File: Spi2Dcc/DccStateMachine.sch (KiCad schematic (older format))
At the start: 9 parts, among them U302 74HC32, U401 74HC163, U402 74HC04, U403 74HC163, U404 74HC193

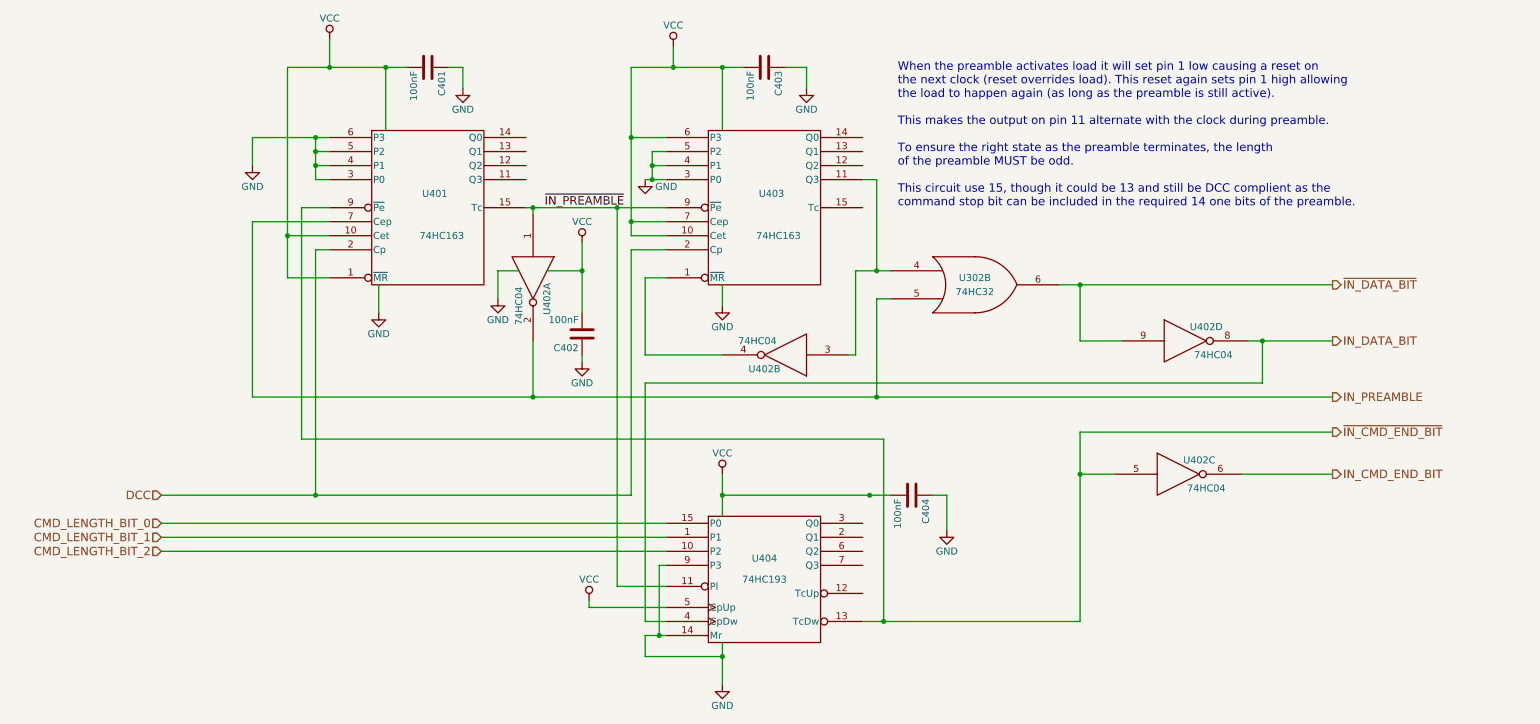
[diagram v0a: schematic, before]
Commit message: Fixed missing connection from U404 to VCC in DccStateMachine schematic. Schematic revision updated to 1.4, pcb not yet.
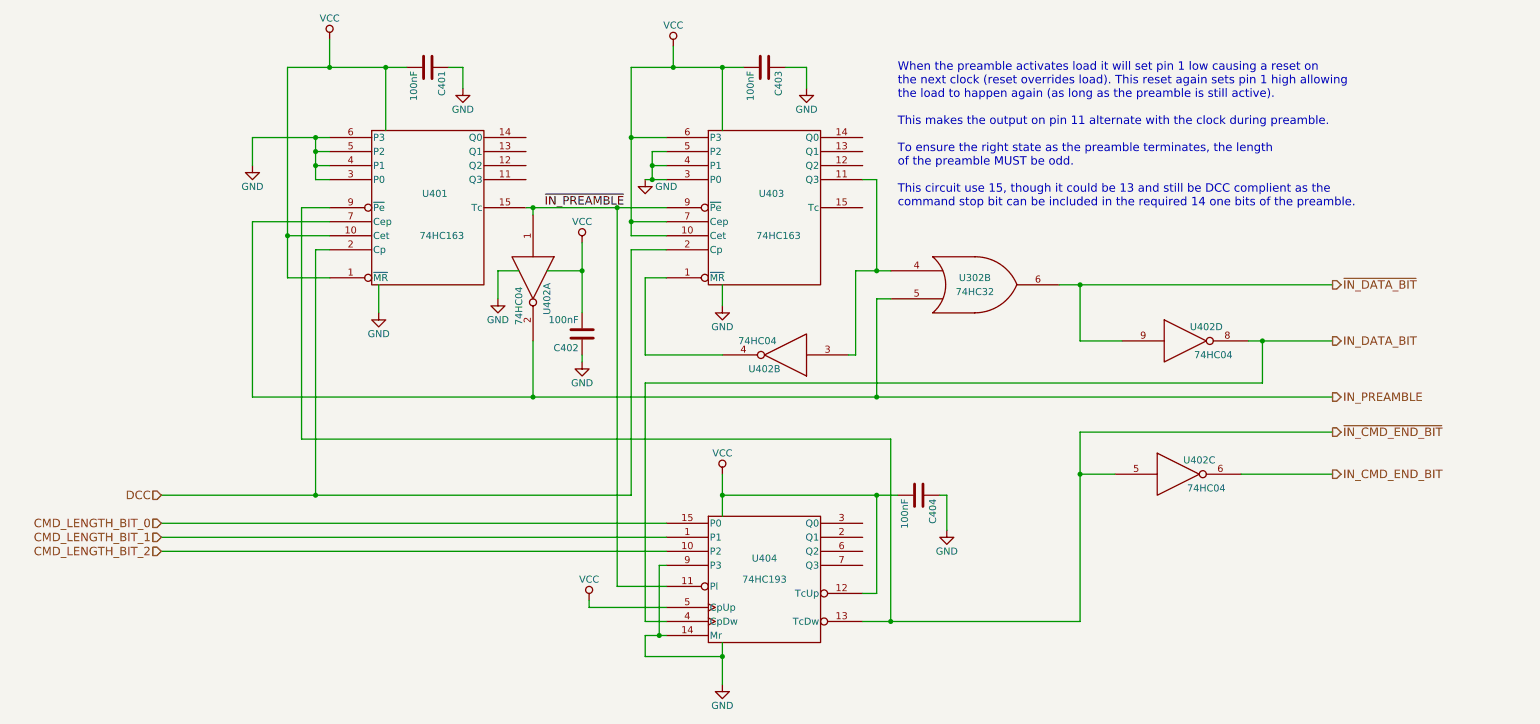
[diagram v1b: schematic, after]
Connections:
- net VCC: now also U404.12 (TcUp)
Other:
- moved on the sheet: C404
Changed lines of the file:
@@
 Sheet 4 9
 Title "Trainiot SPI DCC"
-Date "2017-03-27"
-Rev "1.3"
+Date "2017-04-26"
+Rev "1.4"
 Comp "Lars Møllebjerg"
 Comment1 "The CMD_LENGTH_BITs are used to determine when to generate the command end bit."
@@
 L C C404
 U 1 1 58B3E4A2
-P 7100 4600
-F 0 "C404" H 7125 4700 50  0000 L CNN
-F 1 "100nF" H 7125 4500 50  0000 L CNN
-F 2 "Capacitors_SMD:C_0603" H 7138 4450 50  0001 C CNN
-F 3 "" H 7100 4600 50  0000 C CNN
-	1    7100 4600
+P 7150 4600
+F 0 "C404" H 7175 4700 50  0000 L CNN
+F 1 "100nF" H 7175 4500 50  0000 L CNN
+F 2 "Capacitors_SMD:C_0603" H 7188 4450 50  0001 C CNN
+F 3 "" H 7150 4600 50  0000 C CNN
+	1    7150 4600
 	0    1    1    0
 $EndComp
@@
 	2950 1350 2950 1550
 Wire Wire Line
-	2650 1550 3500 1550
+	2650 1550 2950 1550
+Wire Wire Line
+	2950 1550 3350 1550
+Wire Wire Line
+	3350 1550 3500 1550
 Wire Wire Line
 	3350 1550 3350 2000
 Wire Wire Line
-	2650 1550 2650 3050
+	2650 1550 2650 2750
+Wire Wire Line
+	2650 2750 2650 3050
 Connection ~ 2950 1550
 Wire Wire Line
@@
 	3300 3100 3300 3300
 Wire Wire Line
-	2400 2050 2950 2050
+	2400 2050 2850 2050
+Wire Wire Line
+	2850 2050 2950 2050
 Wire Wire Line
 	2400 2050 2400 2250
@@
 	2950 2150 2850 2150
 Wire Wire Line
-	2850 2050 2850 2350
+	2850 2050 2850 2150
+Wire Wire Line
+	2850 2150 2850 2250
+Wire Wire Line
+	2850 2250 2850 2350
 Connection ~ 2850 2050
 Wire Wire Line
@@
 	3900 1550 3900 1700
 Wire Wire Line
-	4350 2550 5350 2550
+	4350 2550 4400 2550
+Wire Wire Line
+	4400 2550 5000 2550
+Wire Wire Line
+	5000 2550 5350 2550
 Wire Wire Line
 	4400 2550 4400 2600
@@
 	4400 3500 4400 3900
 Wire Wire Line
-	2400 3900 10100 3900
+	2400 3900 4400 3900
+Wire Wire Line
+	4400 3900 6850 3900
+Wire Wire Line
+	6850 3900 10100 3900
 Wire Wire Line
 	2400 3900 2400 2650
@@
 	5750 1550 5750 2000
 Wire Wire Line
-	5100 1550 5900 1550
-Wire Wire Line
-	5100 1550 5100 2750
+	5100 1550 5400 1550
+Wire Wire Line
+	5400 1550 5750 1550
+Wire Wire Line
+	5750 1550 5900 1550
+Wire Wire Line
+	5100 1550 5100 2050
+Wire Wire Line
+	5100 2050 5100 2650
+Wire Wire Line
+	5100 2650 5100 2750
 Wire Wire Line
 	5100 2050 5350 2050
@@
 Connection ~ 5100 2050
 Wire Wire Line
-	1750 4600 5100 4600
+	1750 4600 2850 4600
+Wire Wire Line
+	2850 4600 5100 4600
 Wire Wire Line
 	2850 4600 2850 2850
@@
 	6750 2350 6850 2350
 Wire Wire Line
-	5200 2350 5350 2350
+	5200 2350 5250 2350
+Wire Wire Line
+	5250 2350 5350 2350
 Wire Wire Line
 	5350 2250 5250 2250
 Wire Wire Line
-	5250 2150 5250 2350
+	5250 2150 5250 2250
+Wire Wire Line
+	5250 2250 5250 2350
 Connection ~ 5250 2350
 Wire Wire Line
@@
 	4750 3600 4750 3650
 Wire Wire Line
-	4750 2800 4750 3300
+	4750 2800 4750 3000
+Wire Wire Line
+	4750 3000 4750 3300
 Wire Wire Line
 	4150 3000 4300 3000
@@
 Connection ~ 6850 3900
 Wire Wire Line
-	8150 3100 10100 3100
+	8150 3100 8300 3100
+Wire Wire Line
+	8300 3100 10100 3100
 Wire Wire Line
 	6850 2350 6850 3000
 Wire Wire Line
-	6700 3000 6950 3000
+	6700 3000 6850 3000
+Wire Wire Line
+	6850 3000 6950 3000
 Wire Wire Line
 	1750 4800 5350 4800
@@
 	1750 5000 5350 5000
 Wire Wire Line
-	5750 4450 5750 4750
-Wire Wire Line
-	5750 4600 6950 4600
+	5750 4450 5750 4600
+Wire Wire Line
+	5750 4600 5750 4750
+Wire Wire Line
+	5750 4600 6850 4600
+Wire Wire Line
+	6850 4600 7000 4600
 Connection ~ 5750 4600
 Wire Wire Line
-	7250 4600 7350 4600
+	7300 4600 7350 4600
 Wire Wire Line
 	7350 4600 7350 4850
 Wire Wire Line
-	5750 5650 5750 5950
+	5750 5650 5750 5750
+Wire Wire Line
+	5750 5750 5750 5950
 Wire Wire Line
 	2950 2550 2750 2550
@@
 	2750 2550 2750 4200
 Wire Wire Line
-	8300 5500 6750 5500
-Wire Wire Line
-	6900 5500 6900 4200
-Wire Wire Line
-	6900 4200 2750 4200
+	8300 5500 6950 5500
+Wire Wire Line
+	6950 5500 6750 5500
+Wire Wire Line
+	6950 5500 6950 4200
+Wire Wire Line
+	6950 4200 2750 4200
 Wire Wire Line
 	5000 2550 5000 5250
@@
 	5200 5750 5200 5600
 Wire Wire Line
-	5200 5600 5350 5600
+	5200 5600 5300 5600
+Wire Wire Line
+	5300 5600 5350 5600
 Connection ~ 5750 5750
-Connection ~ 6900 5500
+Connection ~ 6950 5500
 Wire Wire Line
 	10100 4150 8300 4150
@@
 Connection ~ 8300 3100
 Wire Wire Line
-	9500 3500 10100 3500
+	9500 3500 9600 3500
+Wire Wire Line
+	9600 3500 10100 3500
 Wire Wire Line
 	9600 3500 9600 3800
@@
 Wire Wire Line
 	5750 3600 5200 3600
-Connection ~ 6800 4600
-Wire Wire Line
-	8300 4150 8300 5500
+Connection ~ 6850 4600
+Wire Wire Line
+	8300 4150 8300 4450
+Wire Wire Line
+	8300 4450 8300 5500
 $Comp
 L 74HC04 U402
@@
 	4500 3000 4750 3000
 Connection ~ 4750 3000
+Wire Wire Line
+	6850 4600 6850 5300
+Wire Wire Line
+	6850 5300 6750 5300
 $EndSCHEMATC

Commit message: Added NoConnect to unconnected pins
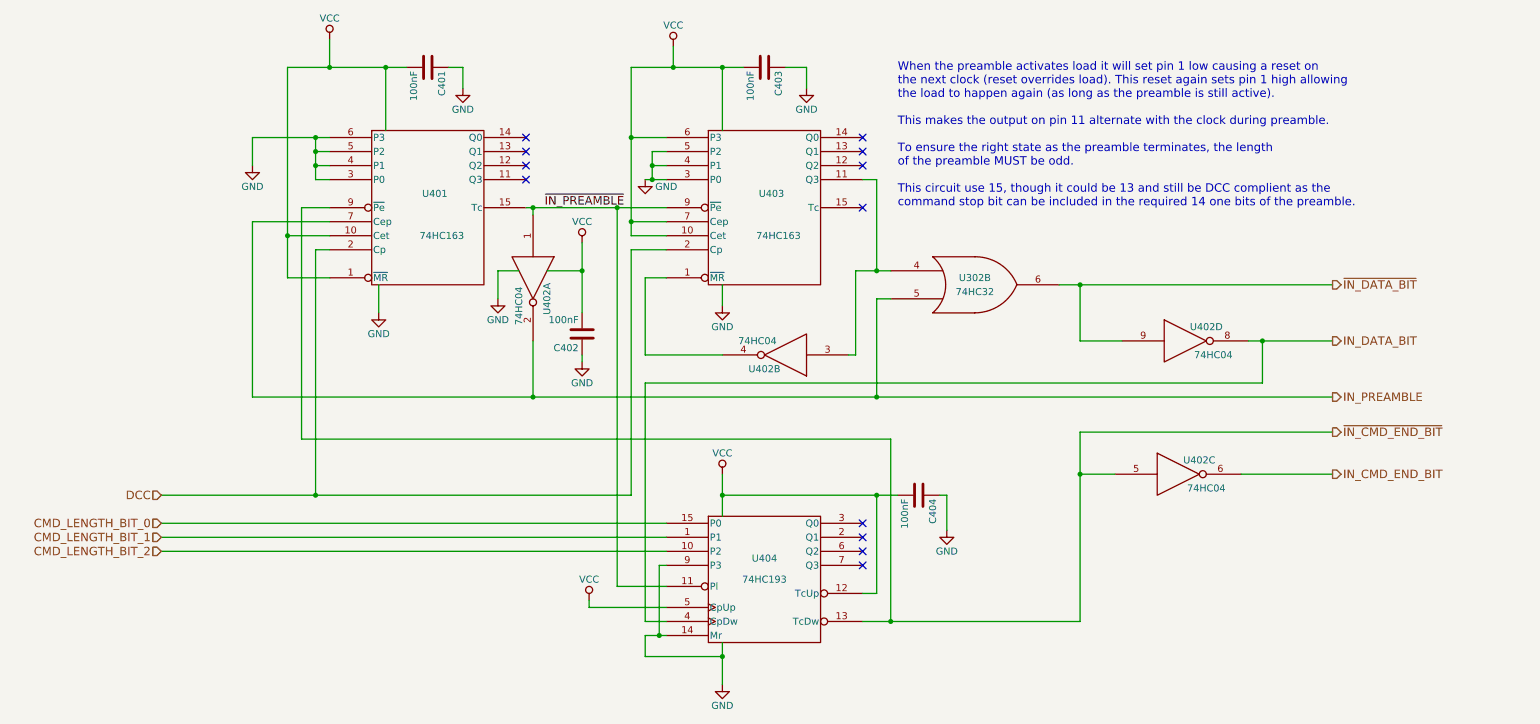
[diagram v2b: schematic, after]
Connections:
- no-connect marks 0 -> 12
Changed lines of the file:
@@
 	2950 1350 2950 1550
 Wire Wire Line
-	2650 1550 2950 1550
-Wire Wire Line
-	2950 1550 3350 1550
-Wire Wire Line
-	3350 1550 3500 1550
+	2650 1550 3500 1550
 Wire Wire Line
 	3350 1550 3350 2000
 Wire Wire Line
-	2650 1550 2650 2750
-Wire Wire Line
-	2650 2750 2650 3050
+	2650 1550 2650 3050
 Connection ~ 2950 1550
 Wire Wire Line
@@
 	3300 3100 3300 3300
 Wire Wire Line
-	2400 2050 2850 2050
-Wire Wire Line
-	2850 2050 2950 2050
+	2400 2050 2950 2050
 Wire Wire Line
 	2400 2050 2400 2250
@@
 	2950 2150 2850 2150
 Wire Wire Line
-	2850 2050 2850 2150
-Wire Wire Line
-	2850 2150 2850 2250
-Wire Wire Line
-	2850 2250 2850 2350
+	2850 2050 2850 2350
 Connection ~ 2850 2050
 Wire Wire Line
@@
 	3900 1550 3900 1700
 Wire Wire Line
-	4350 2550 4400 2550
-Wire Wire Line
-	4400 2550 5000 2550
-Wire Wire Line
-	5000 2550 5350 2550
+	4350 2550 5350 2550
 Wire Wire Line
 	4400 2550 4400 2600
@@
 	4400 3500 4400 3900
 Wire Wire Line
-	2400 3900 4400 3900
-Wire Wire Line
-	4400 3900 6850 3900
-Wire Wire Line
-	6850 3900 10100 3900
+	2400 3900 10100 3900
 Wire Wire Line
 	2400 3900 2400 2650
@@
 	5750 1550 5750 2000
 Wire Wire Line
-	5100 1550 5400 1550
-Wire Wire Line
-	5400 1550 5750 1550
-Wire Wire Line
-	5750 1550 5900 1550
-Wire Wire Line
-	5100 1550 5100 2050
-Wire Wire Line
-	5100 2050 5100 2650
-Wire Wire Line
-	5100 2650 5100 2750
+	5100 1550 5900 1550
+Wire Wire Line
+	5100 1550 5100 2750
 Wire Wire Line
 	5100 2050 5350 2050
@@
 Connection ~ 5100 2050
 Wire Wire Line
-	1750 4600 2850 4600
-Wire Wire Line
-	2850 4600 5100 4600
+	1750 4600 5100 4600
 Wire Wire Line
 	2850 4600 2850 2850
@@
 	6750 2350 6850 2350
 Wire Wire Line
-	5200 2350 5250 2350
-Wire Wire Line
-	5250 2350 5350 2350
+	5200 2350 5350 2350
 Wire Wire Line
 	5350 2250 5250 2250
 Wire Wire Line
-	5250 2150 5250 2250
-Wire Wire Line
-	5250 2250 5250 2350
+	5250 2150 5250 2350
 Connection ~ 5250 2350
 Wire Wire Line
@@
 	4750 3600 4750 3650
 Wire Wire Line
-	4750 2800 4750 3000
-Wire Wire Line
-	4750 3000 4750 3300
+	4750 2800 4750 3300
 Wire Wire Line
 	4150 3000 4300 3000
@@
 Connection ~ 6850 3900
 Wire Wire Line
-	8150 3100 8300 3100
-Wire Wire Line
-	8300 3100 10100 3100
+	8150 3100 10100 3100
 Wire Wire Line
 	6850 2350 6850 3000
 Wire Wire Line
-	6700 3000 6850 3000
-Wire Wire Line
-	6850 3000 6950 3000
+	6700 3000 6950 3000
 Wire Wire Line
 	1750 4800 5350 4800
@@
 	1750 5000 5350 5000
 Wire Wire Line
-	5750 4450 5750 4600
-Wire Wire Line
-	5750 4600 5750 4750
-Wire Wire Line
-	5750 4600 6850 4600
-Wire Wire Line
-	6850 4600 7000 4600
+	5750 4450 5750 4750
+Wire Wire Line
+	5750 4600 7000 4600
 Connection ~ 5750 4600
 Wire Wire Line
@@
 	7350 4600 7350 4850
 Wire Wire Line
-	5750 5650 5750 5750
-Wire Wire Line
-	5750 5750 5750 5950
+	5750 5650 5750 5950
 Wire Wire Line
 	2950 2550 2750 2550
@@
 	2750 2550 2750 4200
 Wire Wire Line
-	8300 5500 6950 5500
-Wire Wire Line
-	6950 5500 6750 5500
+	8300 5500 6750 5500
 Wire Wire Line
 	6950 5500 6950 4200
@@
 	5200 5750 5200 5600
 Wire Wire Line
-	5200 5600 5300 5600
-Wire Wire Line
-	5300 5600 5350 5600
+	5200 5600 5350 5600
 Connection ~ 5750 5750
 Connection ~ 6950 5500
@@
 Connection ~ 8300 3100
 Wire Wire Line
-	9500 3500 9600 3500
-Wire Wire Line
-	9600 3500 10100 3500
+	9500 3500 10100 3500
 Wire Wire Line
 	9600 3500 9600 3800
@@
 Connection ~ 6850 4600
 Wire Wire Line
-	8300 4150 8300 4450
-Wire Wire Line
-	8300 4450 8300 5500
+	8300 4150 8300 5500
 $Comp
 L 74HC04 U402
@@
 Wire Wire Line
 	6850 5300 6750 5300
+NoConn ~ 6750 4800
+NoConn ~ 6750 4900
+NoConn ~ 6750 5000
+NoConn ~ 6750 5100
+NoConn ~ 4350 2050
+NoConn ~ 4350 2150
+NoConn ~ 4350 2250
+NoConn ~ 4350 2350
+NoConn ~ 6750 2050
+NoConn ~ 6750 2150
+NoConn ~ 6750 2250
+NoConn ~ 6750 2550
 $EndSCHEMATC

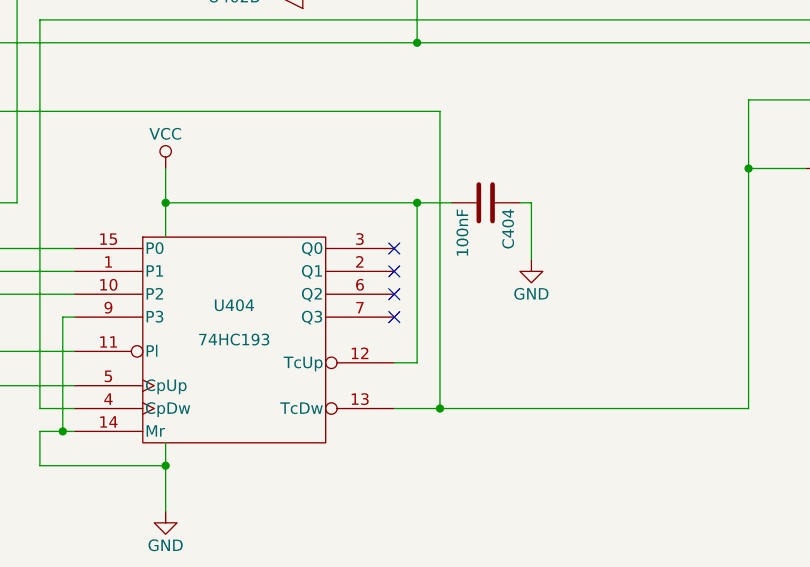
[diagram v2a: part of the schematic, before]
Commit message: Changed back to rev 1.3, update made to 1.4 was invalid.
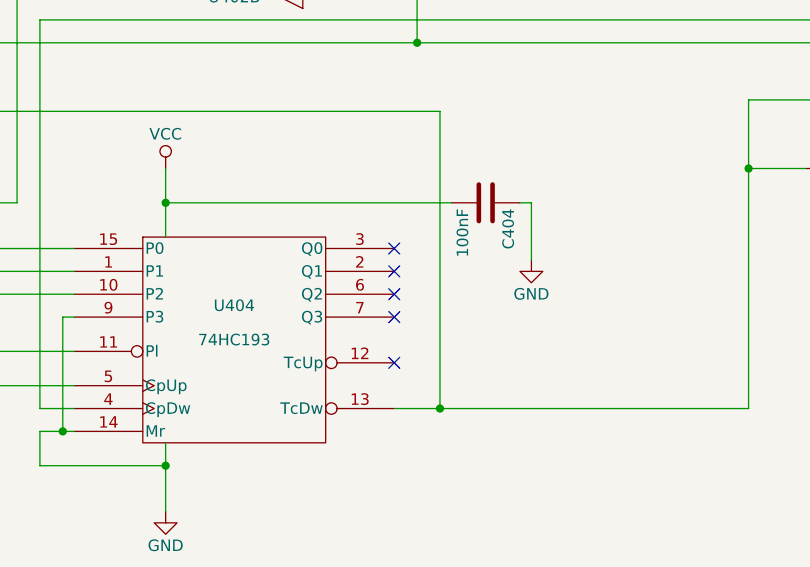
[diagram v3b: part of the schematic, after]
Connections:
- net VCC: no longer U404.12 (TcUp)
- no-connect marks 12 -> 13
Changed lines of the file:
@@
 Title "Trainiot SPI DCC"
 Date "2017-04-26"
-Rev "1.4"
+Rev "1.3"
 Comp "Lars Møllebjerg"
 Comment1 "The CMD_LENGTH_BITs are used to determine when to generate the command end bit."
@@
 Wire Wire Line
 	5750 3600 5200 3600
-Connection ~ 6850 4600
 Wire Wire Line
 	8300 4150 8300 5500
@@
 	4500 3000 4750 3000
 Connection ~ 4750 3000
-Wire Wire Line
-	6850 4600 6850 5300
-Wire Wire Line
-	6850 5300 6750 5300
 NoConn ~ 6750 4800
 NoConn ~ 6750 4900
@@
 NoConn ~ 6750 2250
 NoConn ~ 6750 2550
+NoConn ~ 6750 5300
 $EndSCHEMATC
